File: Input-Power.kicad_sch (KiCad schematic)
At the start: 7 parts, among them Q18 SI2347DS-T1-GE3, Q19 SI2347DS-T1-GE3

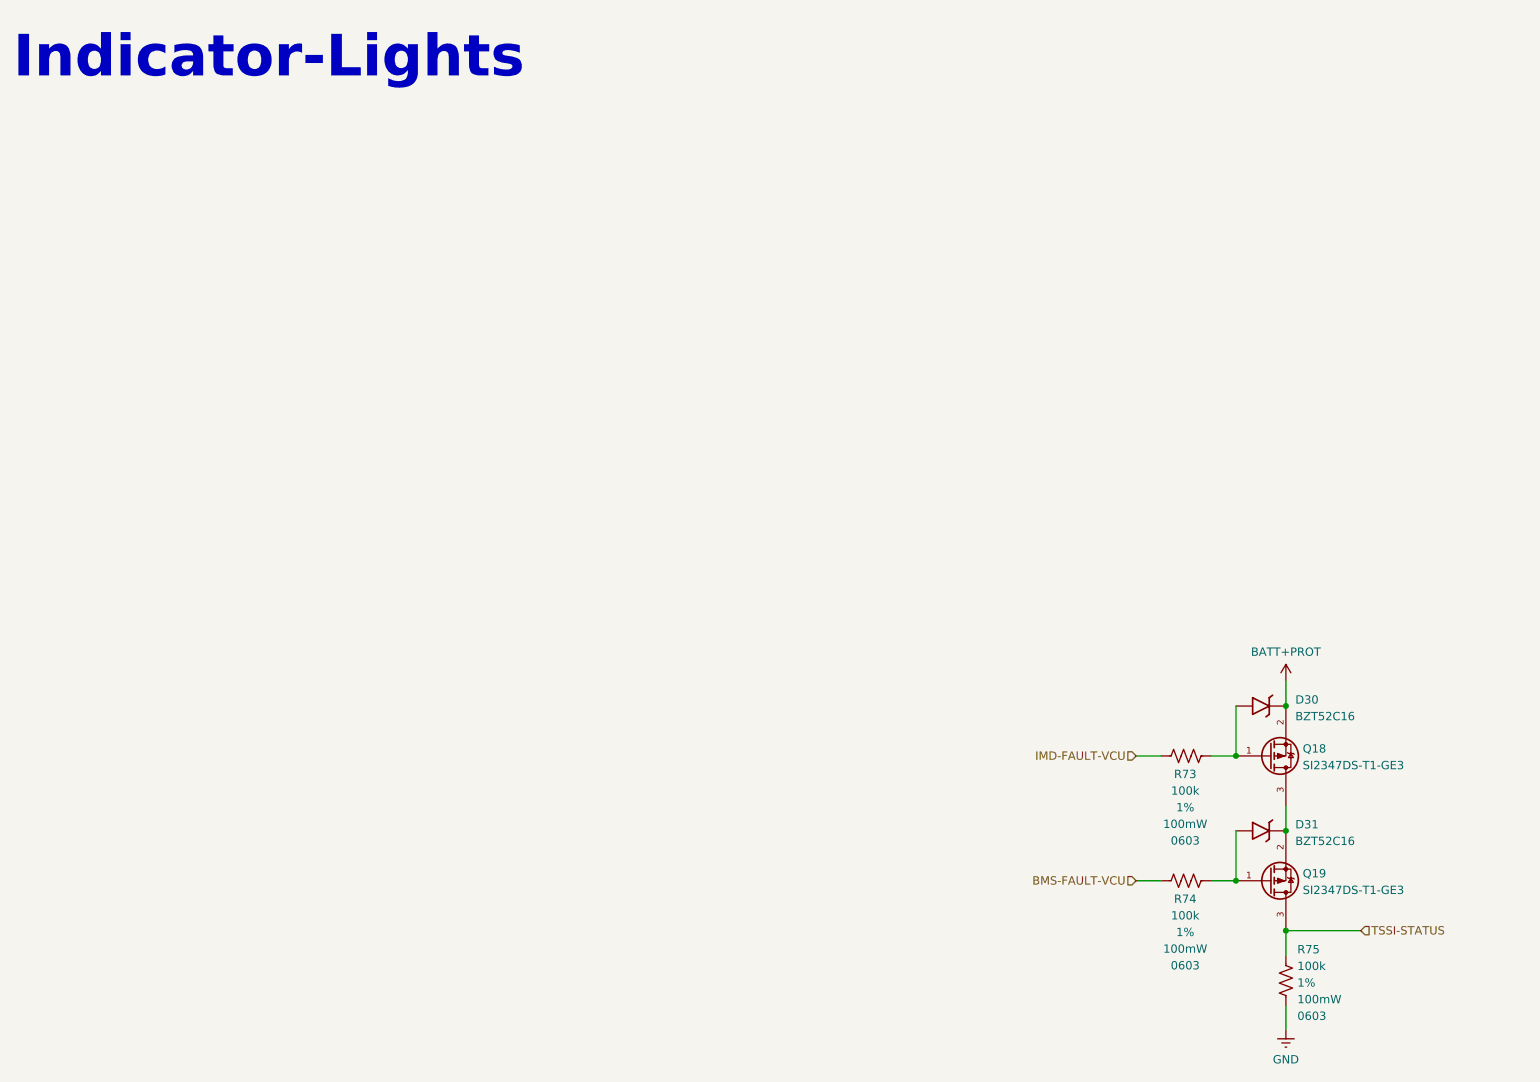
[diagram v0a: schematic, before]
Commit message: completed schematic cleanup, back on 12V
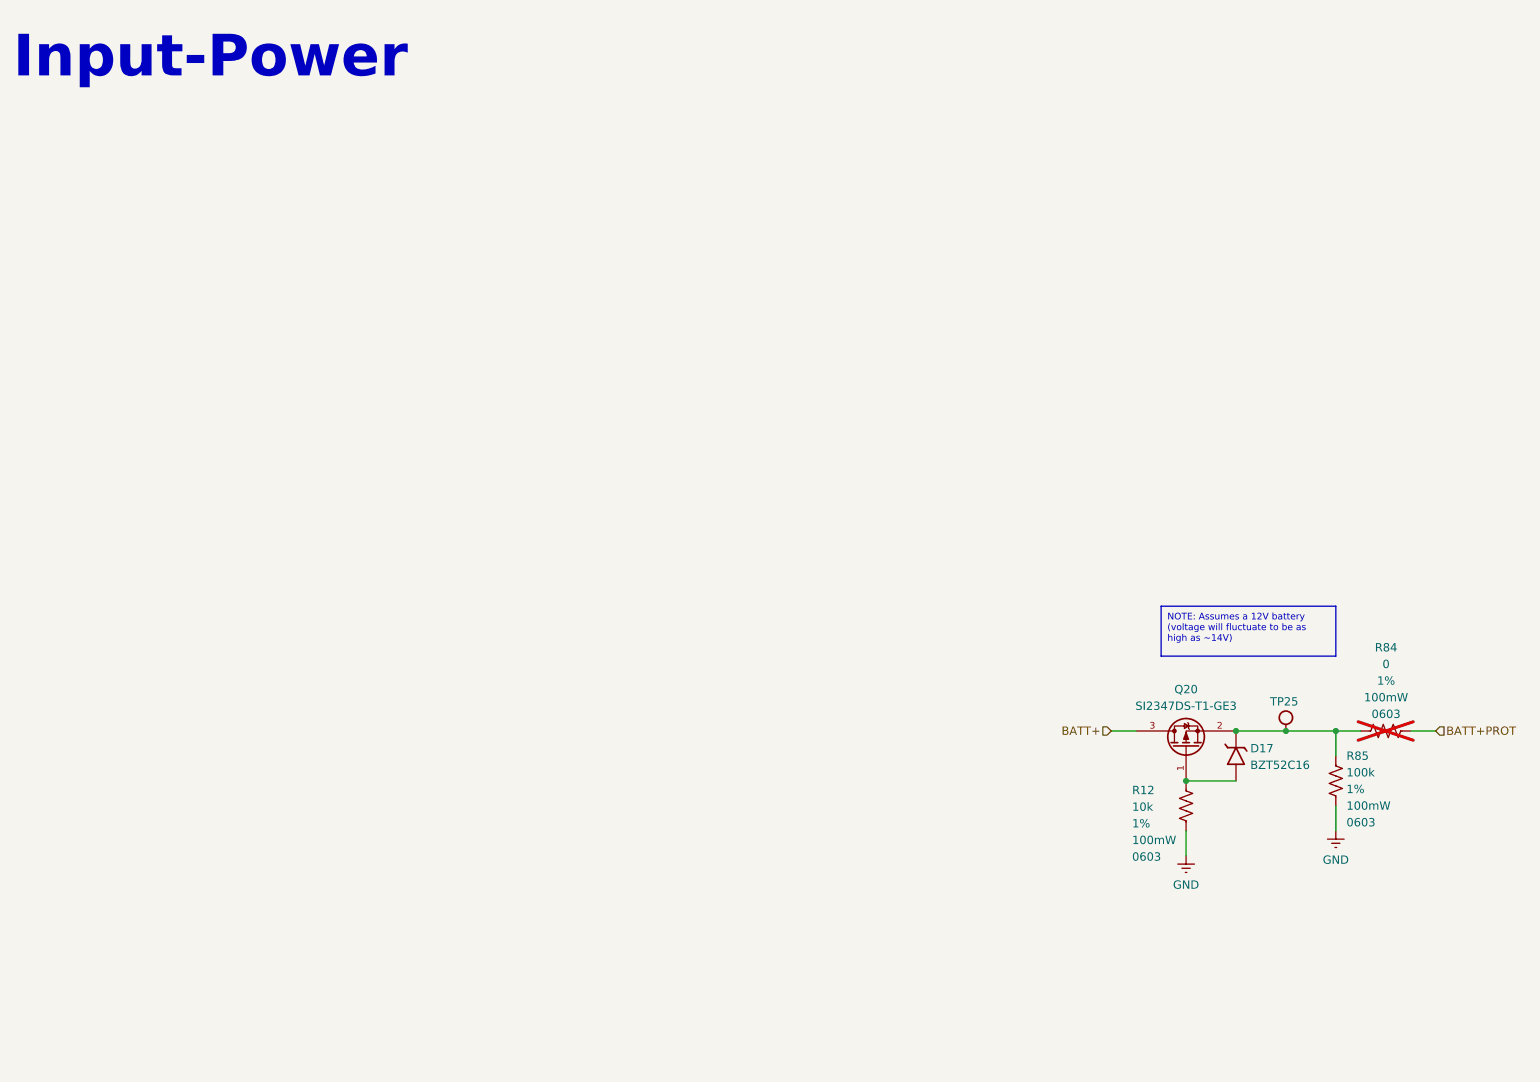
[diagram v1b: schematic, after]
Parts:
- removed D30, D31: BZT52C16, Diode_SMD:D_SOD-123, symbol -Diodes-Zener:BZT52C16
- removed Q18, Q19: SI2347DS-T1-GE3, Package_TO_SOT_SMD:SOT-23-3, symbol -MOSFET-P-Channel:SI2347DS-T1-GE3
- removed R73, R74, R75: 100k, Resistor_SMD:R_0603_1608Metric_Pad0.98x0.95mm_HandSolder, symbol -R-SMD-0603:R-0603-100k-1%-100mW-100PPM
- added D17: BZT52C16, Diode_SMD:D_SOD-123, symbol -Diodes-Zener:BZT52C16
- added Q20: SI2347DS-T1-GE3, Package_TO_SOT_SMD:SOT-23-3, symbol -MOSFET-P-Channel:SI2347DS-T1-GE3
- added R12: 10k, Resistor_SMD:R_0603_1608Metric_Pad0.98x0.95mm_HandSolder, symbol -R-SMD-0603:R-0603-10k-1%-100mW-100PPM
- added R84: 0, Resistor_SMD:R_0603_1608Metric_Pad0.98x0.95mm_HandSolder, symbol -R-SMD-0603:R-0603-0-1%-100mW-1500PPM
- added R85: 100k, Resistor_SMD:R_0603_1608Metric_Pad0.98x0.95mm_HandSolder, symbol -R-SMD-0603:R-0603-100k-1%-100mW-100PPM
- added TP25: ~, TestPoint:TestPoint_Pad_1.0x1.0mm, symbol -Test-Points:Square-Pad-1mm
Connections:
- net BATT+PROT: now also R84.2
- net GND: now also R12.1, R85.1
- new net: D17.1 (K), Q20.2 (S), R84.1, R85.2, TP25.1
- new net: D17.2 (A), Q20.1 (G), R12.2
- new net BATT+: Q20.3 (D)
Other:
- note added: "Input-Power"
- note removed: "Indicator-Lights"
